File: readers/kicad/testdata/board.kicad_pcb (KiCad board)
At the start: 2 copper layers, 32 x 20 mm, 4 parts, among them J1 CONN

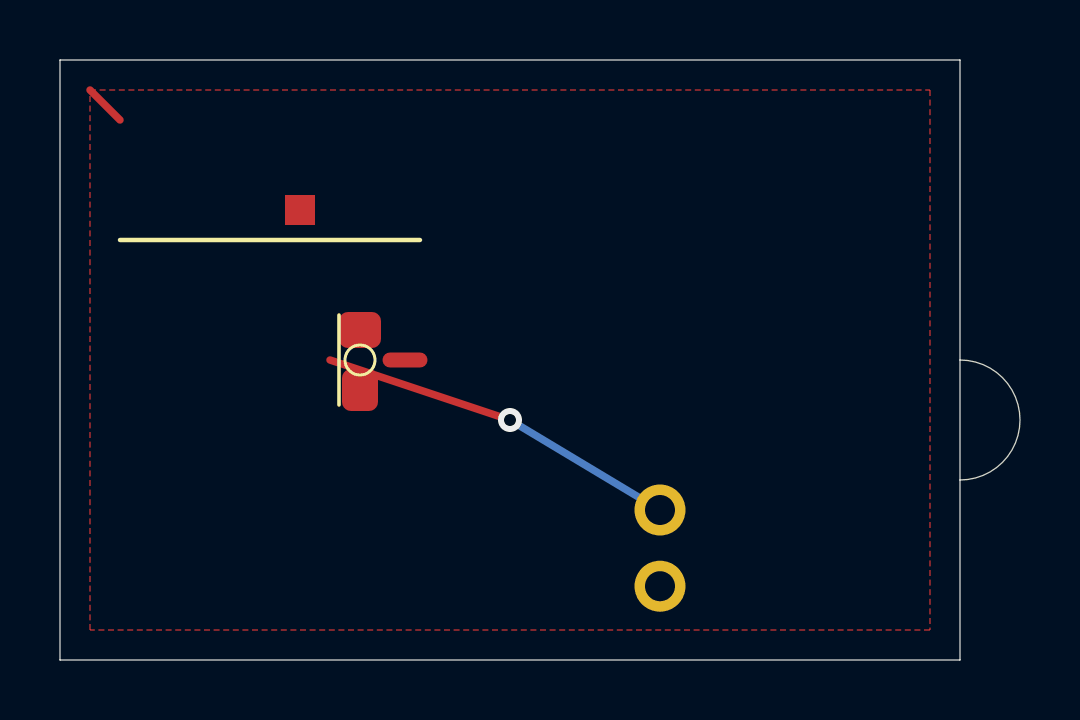
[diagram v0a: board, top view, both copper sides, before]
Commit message: readers/kicad: use the shared placeholder-designator predicate
The KiCad reader carried its own `placeholderRef`, matching "?" only as a suffix, while
`internal/refdes.IsPlaceholder` matches it anywhere. A partly-assigned "C?1845" was
therefore a placeholder to one layer and a real designator to the other, which is the
uneven application agni issue 311 names.

This is a behaviour change to board reads, which is why PR 310 left it alone: a footprint
whose reference has a mid-name "?" now gets skipped by the netlist reader, the
board-geometry reader and the silk-text pass, the same way "REF**" already was. On the
schematic side an `instances` entry with such a reference is no longer taken as
post-annotation truth, so the symbol falls back to its property and stays visibly
unannotated instead of acquiring "C?1845" as an identity.

The two fixtures gain the partly-assigned form beside the fully unassigned one they
already carried. Both new assertions were confirmed red with the predicate narrowed back
to a suffix match.
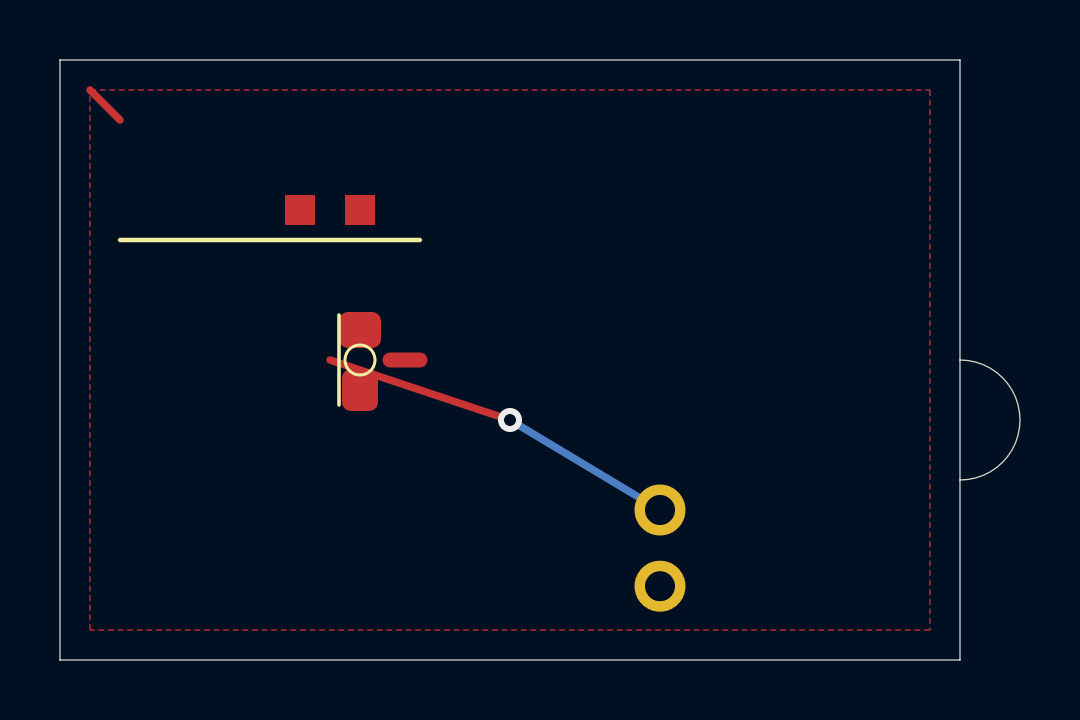
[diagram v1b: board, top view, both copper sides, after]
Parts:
- added C?1845: , Capacitor_SMD:C_0603, F.Cu at (10.0, 5.00)
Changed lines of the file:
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@@
 			(at 0 -2 0))
 		(pad "1" smd rect (at 0 0) (size 1 1) (layers "F.Cu") (net 1 "GND") (uuid "p-ph1")))
+	(footprint "Capacitor_SMD:C_0603"
+		(layer "F.Cu")
+		(uuid "fp-ph2")
+		(at 10 5)
+		(property "Reference" "C?1845"
+			(at 0 -2 0))
+		(pad "1" smd rect (at 0 0) (size 1 1) (layers "F.Cu") (net 1 "GND") (uuid "p-ph2")))
 	(segment (start 9 10) (end 15 12) (width 0.25) (layer "F.Cu") (net 2) (uuid "s1"))
 	(segment (start 15 12) (end 20 15) (width 0.25) (layer "B.Cu") (net 2) (uuid "s2"))
